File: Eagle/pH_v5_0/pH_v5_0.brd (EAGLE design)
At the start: 100 x 84.6 mm, 136 parts, among them CON1 JACK_DC_BARREL, IC1 MCP1703DB, IC3 SN74LVC2G14, J1 RJ12RIGHTANGLE-I2C, J2 RJ12RIGHTANGLE-I2C, J7 22--02, Q1 BSP75, Q2 BSP75, Q3 BSP75, Q4 BSP75, Q5 BSP75, Q6 BSP75, U1 HX711, U100 RN2483, X2 16MHz, X3 FH12-08S-1SH, X4 MINI-USB

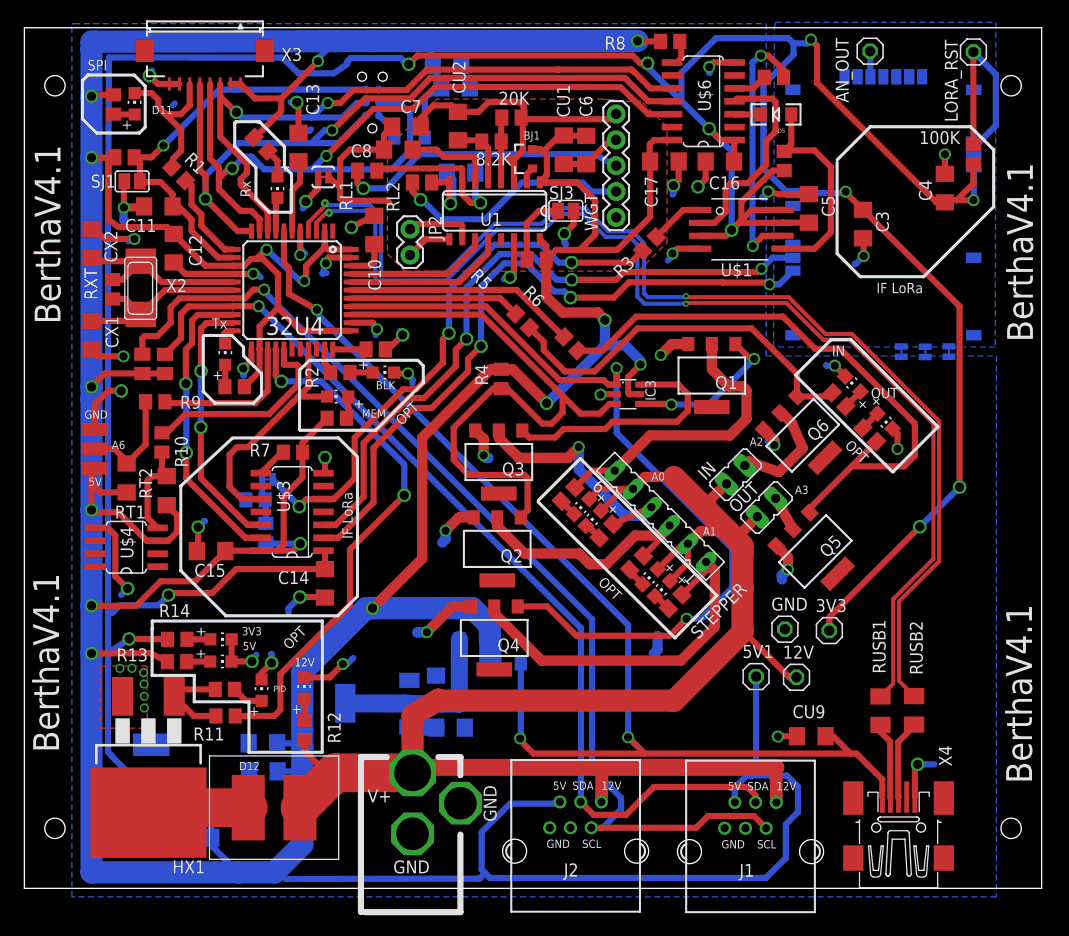
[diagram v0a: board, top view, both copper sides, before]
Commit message: started pH conducto PCB board
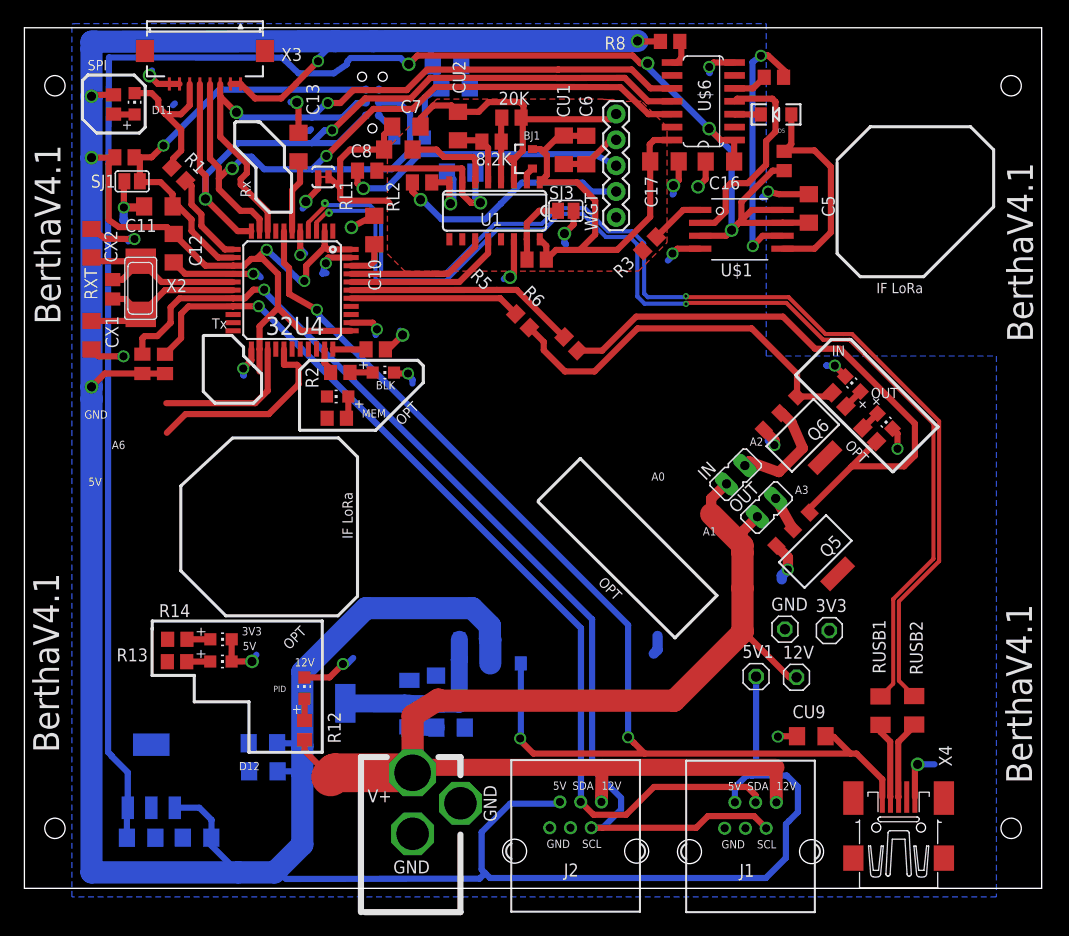
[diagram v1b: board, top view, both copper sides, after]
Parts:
- removed 100K: 100k, rcl:R0805
- removed 5K: 5k, rcl:R0805
- removed AN_OUT, LORA_RST: (no value), Headerlibrary:1X01
- removed C14, C15, C3, C4: 100nF, rcl:C1206
- removed HX1: IRF3704S, transistor-power:D2PACK
- removed IC3: SN74LVC2G14, lpatiny:SOT23-6
- removed J7: 22--02, lpatiny:2-PIN-5.08S
- removed JP2: (no value), SparkFun-Connectors:1X02
- removed LDM1, LDM2, LDM3, LDM4, LDPID, RXLD, TXLD: RED, adafruit:CHIP-LED0805
- removed Q1, Q2, Q3, Q4: BSP75, infineon:PG-SOT-223
- removed R10, R11, R4, R7, R9: 1K, rcl:R0805
- removed RK10, RK11, RK8, RK9: 10K, rcl:R0805
- removed RK14, RK15, RK16, RK17: 10k, rcl:R0805
- removed RT1, RT2: 4.7k, resistor:R1206
- removed SJ4, SJ5, SJ6, SJ7: (no value), SparkFun-Passives:PAD-JUMPER-2-NC_BY_TRACE_YES_SILK
- removed STEPPER: (no value), con-lsta:FE06
- removed U$3: TXB0104, lpatiny:SO14
- removed U$4: DS18B20, lpatiny:SO8
- removed U$8: DS18B20_SMALLPADS, lpatiny:SMALLPADS_X3
- removed U100: RN2483, Octanis1:RN2483
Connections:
- removed net ANGND: C3.2, C4.2, SJ4.2, SJ5.2, SJ6.2, U100.P$1, U100.P$11, U100.P$20, U100.P$21, U100.P$22, U100.P$24, U100.P$26, U100.P$27, U100.P$28, U100.P$33, U100.P$41, U100.P$47, U100.P$8
- removed net ANT868: AN_OUT.1, U100.P$23
- removed net B+: JP2.1, U1.10
- removed net B-: JP2.2, U1.9
- removed net LORA_RST: 100K.2, LORA_RST.1, U100.P$32
- removed net N$14: Q4.2, RK8.1, STEPPER.1
- removed net N$15: Q2.2, RK9.1, STEPPER.3
- removed net N$16: Q3.2, RK10.1, STEPPER.4
- removed net N$18: RK15.2, TXLD.A
- removed net N$19: Q1.2, RK11.1, STEPPER.6
- removed net N$2: R7.1, U$3.8
- removed net N$21: R9.2, RT1.2, U$8.PIN2
- removed net N$24: RK16.2, RXLD.A
- removed net N$26: LDPID.A, RK14.1
- removed net N$29: IC3.6, Q3.1
- removed net N$30: IC3.4, Q1.1
- removed net N$31: LDM4.C, RK8.2
- removed net N$32: LDM3.C, RK9.2
- removed net N$33: LDM2.C, RK10.2
- removed net N$35: 5K.1, RK17.2, SJ7.2
- removed net N$36: HX1.2, J7.2
- removed net N$37: LDM1.C, RK11.2
- removed net N$6: HX1.1, R11.2, RK14.2
- removed net N$9: R10.2, RT2.2, U$4.4
- removed net RX3: U$3.2, U100.P$6
- removed net TX3: U$3.3, U100.P$7
- net +12V: no longer J7.1, LDM1.A, LDM2.A, LDM3.A, LDM4.A, STEPPER.2, STEPPER.5
- net +5V/1: no longer C15.2, IC3.5, R4.2, R7.2, RK15.1, RK16.1, RK17.1, RT1.1, RT2.1, U$3.14, U$4.3, U$8.PIN3
- net 3.3V: no longer 100K.1, C14.2, C3.1, C4.1, U$3.1, U100.P$12, U100.P$34
- net A0: no longer IC3.3, Q2.1, R4.1
- net A1: no longer IC3.1, Q4.1
- net A6: no longer R9.1
- net D10*: now also U$6.9; no longer U$3.10
- net D12*: no longer R11.1
- net D6*: no longer R10.1
- net GND: no longer 5K.2, C14.1, C15.1, HX1.3, IC3.2, LDPID.C, Q1.3, Q2.3, Q3.3, Q4.3, SJ4.1, SJ5.1, SJ6.1, U$3.7, U$4.5, U$8.PIN1
- net RX: no longer U$3.13
- net RXLED: no longer RXLD.C
- net SC_MEM: now also U$6.6; no longer SJ7.1, U$3.5
- net TX: no longer U$3.12
- net TXLED: no longer TXLD.C
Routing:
- net 3.3V: track 339.2 -> 182.3 mm, vias 11 -> 4
- net +5V/1: track 594.1 -> 451.3 mm, vias 15 -> 7
- net A1: track 81.4 -> 0.00 mm, vias 2 -> 0
- net RX3: track 67.3 -> 0.00 mm, vias 3 -> 0
- net TX3: track 66.1 -> 0.00 mm, vias 3 -> 0
- net A0: track 61.7 -> 0.00 mm
- net SC_MEM: track 55.6 -> 0.00 mm, vias 3 -> 0
- net D12*: track 52.8 -> 0.00 mm, vias 2 -> 0
- net GND: track 171.0 -> 124.0 mm, vias 46 -> 29
- net N$14: track 36.6 -> 0.00 mm
- net +12V: track 169.0 -> 133.3 mm
- net RX: track 29.8 -> 0.00 mm, vias 2 -> 0
- net N$19: track 29.2 -> 0.00 mm
- net TX: track 25.9 -> 0.00 mm, vias 2 -> 0
- net N$16: track 25.5 -> 0.00 mm, vias 1 -> 0
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- removed copper zone on layer 16, net ANGND
- removed copper zone on layer 1, net GND
